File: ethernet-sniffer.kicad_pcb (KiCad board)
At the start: 4 copper layers, 120 x 117 mm, 320 parts, among them J1001 RJMG1BD3B8K1ANR, J101 Conn_01x06, J102 USB_B_Micro, J103 POWER 5V, J1101 RJMG1BD3B8K1ANR, J601 BOOT0, J602 BOOT1, J603 Debug Header, J606 Exension Port D, J701 JTAG, J801 RJMG1BD3B8K1ANR, J901 RJMG1BD3B8K1ANR, Q201 2N3904, Q202 2N3904, Q701 2N3904, SW601 SW_Push, SW701 RESET, U1001 AMS1117-3.3, U1002 DP83848C, U1101 AMS1117-3.3, U1102 DP83848C, U501 CH340G, U601 AMS1117-3.3, U602 STM32F107VCTx, U701 LM317_3PinPackage, U702 AMS1117-3.3, U707 XC6SLX9-TQG144, U708 W25Q128JVS, U801 AMS1117-3.3, U802 DP83848C, U901 AMS1117-3.3, U902 DP83848C, Y501 12MHz, Y601 25MHz

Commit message: Cleanup
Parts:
- added REF**: OSHW-Logo2_36.5x30mm_SilkScreen, Symbol:OSHW-Logo2_36.5x30mm_SilkScreen, B.Cu at (114.2, 125.2)
- J101: value Conn_01x06 -> Conn_01x08; footprint Connector_PinHeader_2.54mm:PinHeader_1x06_P2.54mm_Vertical -> Connector_PinHeader_2.54mm:PinHeader_1x08_P2.54mm_Vertical
- moved J101 17.8 mm to (210.0, 100.2), turned to 0 degrees
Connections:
- J101 pad 1: /STM32/UART_TX -> GNDD
- J101 pad 2: /STM32/UART_RX -> /STM32/STM_3V3
- J101 pad 3: /STM32/ADC1 -> /STM32/I2C_SCL
- J101 pad 4: /STM32/ADC2 -> /STM32/I2C_SDA
- J101 pad 5: /STM32/I2C_SDA -> /STM32/ADC2
- J101 pad 6: /STM32/I2C_SCL -> /STM32/ADC1
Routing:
- net /STM32/I2C_SDA: track 39.7 -> 34.6 mm
- net /STM32/STM_3V3: track 39.2 -> 44.0 mm
- net /STM32/I2C_SCL: track 37.3 -> 39.6 mm
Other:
- board text added: "3V3"
- board text added: "ADC1"
- board text added: "ADC2"
- board text added: "BOOT0"
- board text added: "BOOT1"
- board text added: "Christopher Simon"
- board text added: "Ethernet Sniffer v0.01"
- board text added: "FPGA 100BASE-TX 1"
- board text added: "FPGA 100BASE-TX 2"
- board text added: "FPGA 100BASE-TX 3"
- board text added: "GND"
- board text added: "JTAG"
- board text added: "PD0-7"
- board text added: "SDA"
- board text added: "SDL"
- board text added: "STM32 100BASE-TX"
- board text added: "SWD"
- board text added: "UART RX"
- board text added: "UART TX"

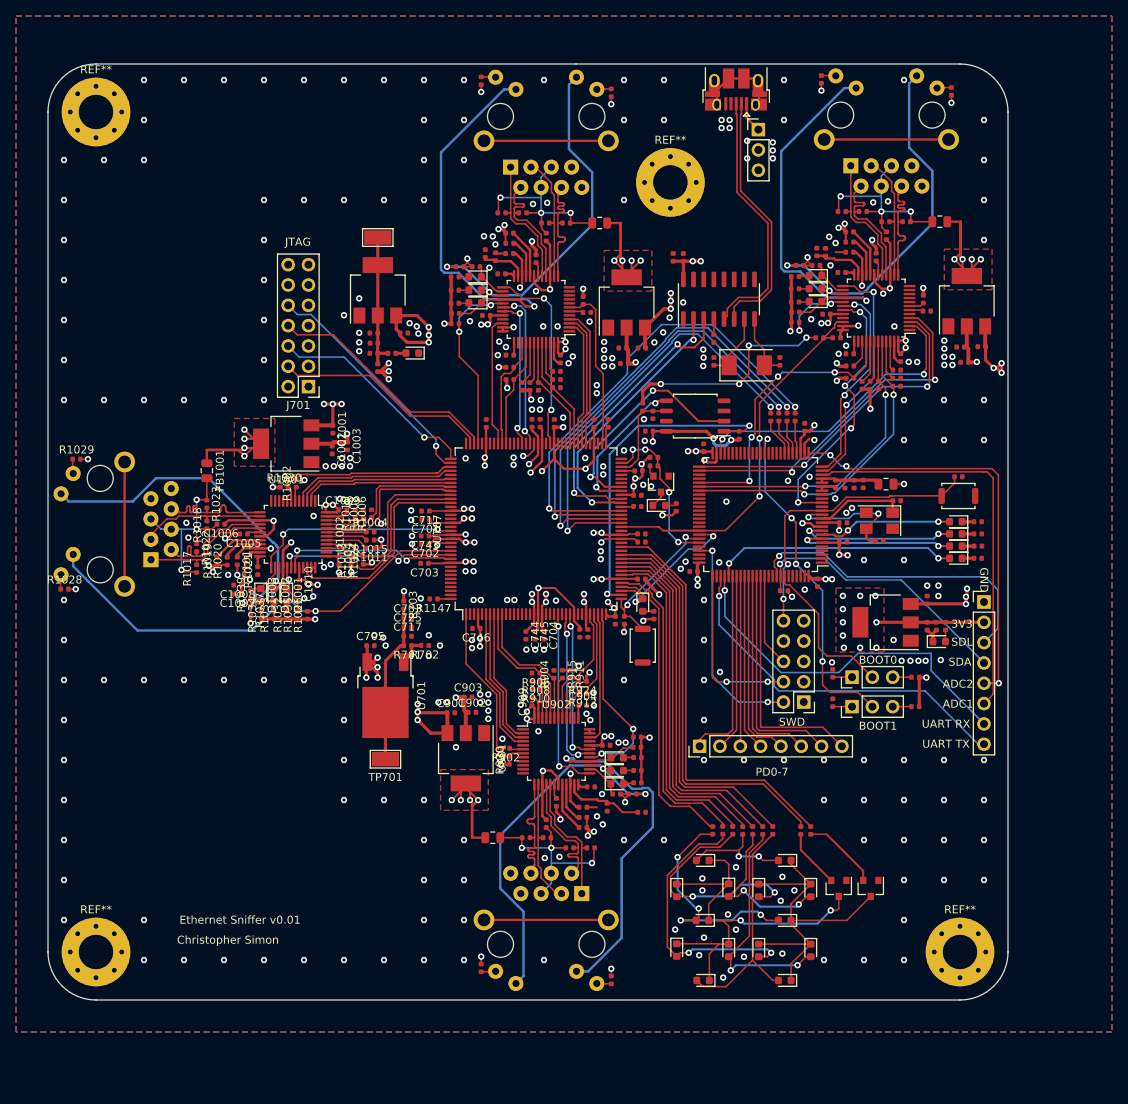
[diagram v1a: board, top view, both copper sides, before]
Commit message: PCB layout 90% finished
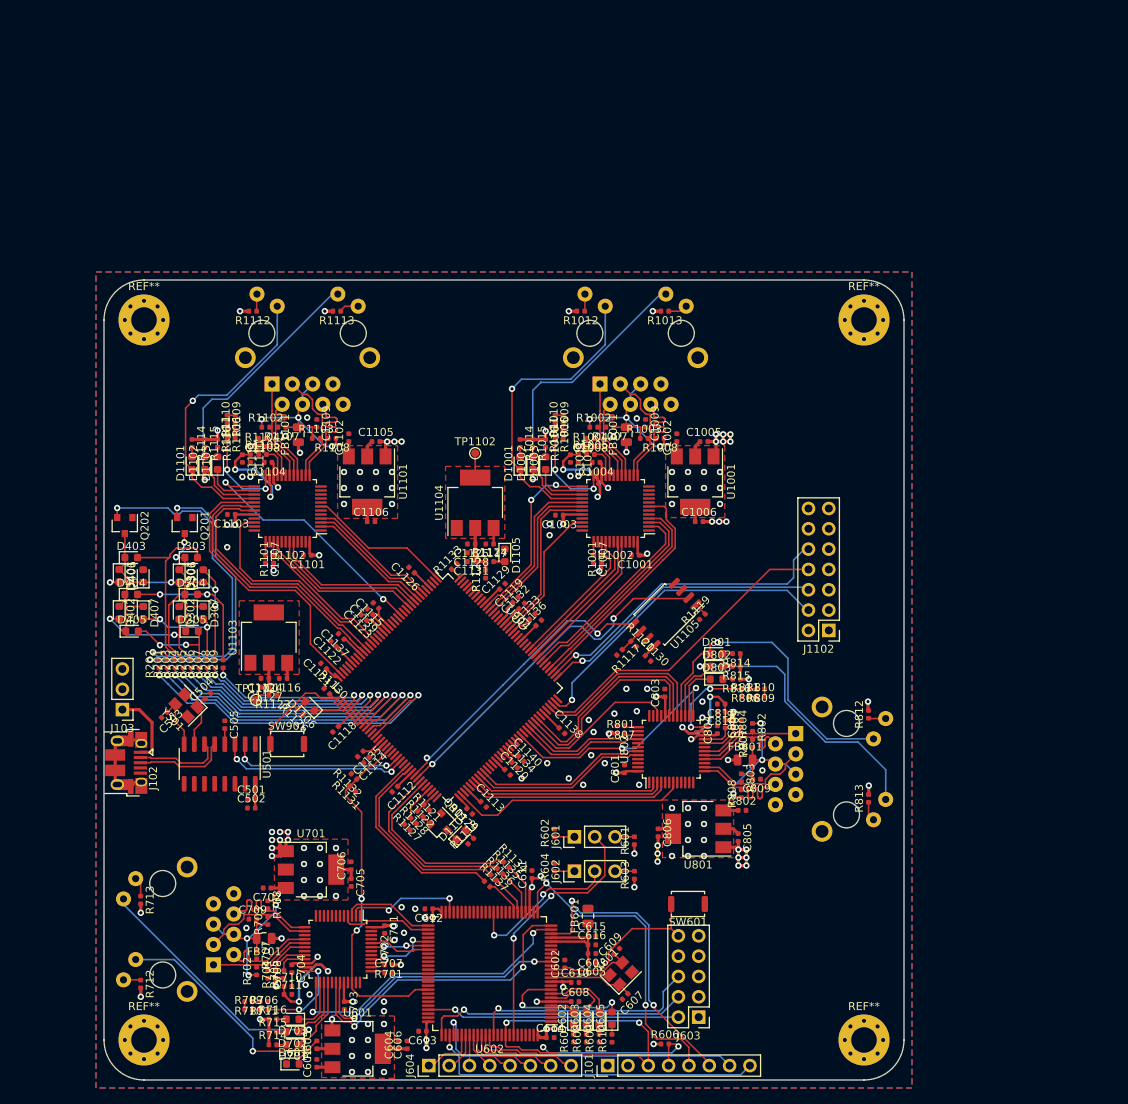
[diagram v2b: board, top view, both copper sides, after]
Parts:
- removed C1012, C712, C713, C714, C715, C716, C723, C724, C732, C740, C741, C743, C744, C745, C746, C747, C748, C903, C904, C905, C906, C907, C909, C910, C911: 100n, Capacitor_SMD:C_0402_1005Metric
- removed C717, C718, C901, C908: 10u, Capacitor_SMD:C_0402_1005Metric
- removed C725, C726: 4u7, Capacitor_SMD:C_0402_1005Metric
- removed C733, C734: 470n, Capacitor_SMD:C_0402_1005Metric
- removed C902: 1u, Capacitor_SMD:C_0402_1005Metric
- removed D706, D707: INIT, LED_SMD:LED_0603_1608Metric
- removed D901: LINK, LED_SMD:LED_0603_1608Metric
- removed D902: SPEED, LED_SMD:LED_0603_1608Metric
- removed D903: ACT, LED_SMD:LED_0603_1608Metric
- removed FB901: Bead, Inductor_SMD:L_0805_2012Metric
- removed J606: Exension Port D, Connector_PinHeader_2.54mm:PinHeader_1x08_P2.54mm_Vertical
- removed J901: RJMG1BD3B8K1ANR, Connector_RJ:RJ45_Amphenol_RJMG1BD3B8K1ANR
- removed Q701: 2N3904, Package_TO_SOT_SMD:SOT-23
- removed R1017, R1018, R1022, R1023, R817, R818, R822, R823, R917, R918, R922, R923: 50, Resistor_SMD:R_0402_1005Metric
- removed R1019, R1020, R1024, R1026, R1030, R1035, R1037, R1039, R1139, R1147, R1148, R719, R721, R722, R723, R819, R820, R824, R826, R830, R835, R837, R839, R902, R904, R906, R908, R910, R911, R913, R915, R919, R920, R924, R926, R930, R935, R937, R939: 2k2, Resistor_SMD:R_0402_1005Metric
- removed R1021, R821, R921: 4k87, Resistor_SMD:R_0402_1005Metric
- removed R1028, R1029, R1032, R1033, R1034, R720, R828, R829, R832, R833, R834, R928, R929, R932, R933, R934: 200, Resistor_SMD:R_0402_1005Metric
- removed R1141, R1142, R717: 100, Resistor_SMD:R_0402_1005Metric
- removed R1143, R1144, R1145, R1146: 1k, Resistor_SMD:R_0402_1005Metric
- removed R718: 10k, Resistor_SMD:R_0402_1005Metric
- removed the REF** at (114.2, 125.2)
- removed the REF** at (170.8, 47.8)
- removed the REF** at (207.0, 144.0)
- removed the REF** at (99.0, 144.0)
- removed the REF** at (99.0, 39.0)
- removed SW701: RESET, Button_Switch_SMD:SW_Push_SPST_NO_Alps_SKRK
- removed TP701: TP 1.2V VCCINT, TestPoint:TestPoint_Keystone_5015_Micro-Minature
- removed TP702: TP 3.3V VCCAUX, TestPoint:TestPoint_Keystone_5015_Micro-Minature
- removed U707: XC6SLX9-TQG144, Package_QFP:LQFP-144_20x20mm_P0.5mm
- removed U708: W25Q128JVS, Package_SO:SOIC-8_5.23x5.23mm_P1.27mm
- removed U901: AMS1117-3.3, Package_TO_SOT_SMD:SOT-223-3_TabPin2
- removed U902: DP83848C, Package_QFP:LQFP-48_7x7mm_P0.5mm
- added C1112: 100n, Capacitor_SMD:C_0402_1005Metric, F.Cu at (136.4, 123.6)
- added C1113: 100n, Capacitor_SMD:C_0402_1005Metric, F.Cu at (147.4, 125.5)
- added C1114: 100n, Capacitor_SMD:C_0402_1005Metric, F.Cu at (132.8, 120.0)
- added C1115: 100n, Capacitor_SMD:C_0402_1005Metric, F.Cu at (134.0, 100.7)
- added C1116: 4u7, Capacitor_SMD:C_0402_1005Metric, F.Cu at (122.4, 109.8)
- added C1117: 4u7, Capacitor_SMD:C_0402_1005Metric, F.Cu at (148.2, 93.0)
- added C1118: 100n, Capacitor_SMD:C_0402_1005Metric, F.Cu at (128.9, 116.2)
- added C1119: 100n, Capacitor_SMD:C_0402_1005Metric, F.Cu at (151.4, 100.0)
- added C1120: 100n, Capacitor_SMD:C_0402_1005Metric, F.Cu at (150.4, 121.5)
- added C1121: 100n, Capacitor_SMD:C_0402_1005Metric, F.Cu at (127.5, 108.3)
- added C1122: 100n, Capacitor_SMD:C_0402_1005Metric, F.Cu at (128.7, 105.5)
- added C1123: 100n, Capacitor_SMD:C_0402_1005Metric, F.Cu at (132.5, 102.2)
- added C1124: 10u, Capacitor_SMD:C_0402_1005Metric, F.Cu at (120.1, 109.8)
- added C1125: 10u, Capacitor_SMD:C_0402_1005Metric, F.Cu at (145.9, 93.0)
- added C1126: 100n, Capacitor_SMD:C_0402_1005Metric, F.Cu at (138.5, 96.3)
- added C1127: 4u7, Capacitor_SMD:C_0402_1005Metric, F.Cu at (120.1, 110.9)
- added C1128: 4u7, Capacitor_SMD:C_0402_1005Metric, F.Cu at (145.9, 94.1)
- added C1129: 100n, Capacitor_SMD:C_0402_1005Metric, F.Cu at (149.8, 98.3)
- added C1130: 100n, Capacitor_SMD:C_0402_1005Metric, F.Cu at (168.0, 107.3)
- added C1131: 470n, Capacitor_SMD:C_0402_1005Metric, F.Cu at (145.9, 95.2)
- added C1132: 100n, Capacitor_SMD:C_0402_1005Metric, F.Cu at (152.2, 100.8)
- added C1133: 100n, Capacitor_SMD:C_0402_1005Metric, F.Cu at (153.5, 102.1)
- added C1134: 100n, Capacitor_SMD:C_0402_1005Metric, F.Cu at (151.3, 120.6)
- added C1135: 100n, Capacitor_SMD:C_0402_1005Metric, F.Cu at (132.1, 119.2)
- added C1136: 100n, Capacitor_SMD:C_0402_1005Metric, F.Cu at (154.3, 102.9)
- added C1137: 100n, Capacitor_SMD:C_0402_1005Metric, F.Cu at (129.7, 104.6)
- added C1138: 100n, Capacitor_SMD:C_0402_1005Metric, F.Cu at (157.2, 116.3)
- added C1139: 100n, Capacitor_SMD:C_0402_1005Metric, F.Cu at (133.3, 101.5)
- added C1140: 100n, Capacitor_SMD:C_0402_1005Metric, F.Cu at (152.1, 119.8)
- added C707: 100n, Capacitor_SMD:C_0402_1005Metric, F.Cu at (135.6, 146.6)
- added C708: 100n, Capacitor_SMD:C_0402_1005Metric, F.Cu at (120.5, 146.8)
- added C709: 100n, Capacitor_SMD:C_0402_1005Metric, F.Cu at (118.6, 139.9)
- added C710: 100n, Capacitor_SMD:C_0402_1005Metric, F.Cu at (123.0, 148.3)
- added D1104: INIT, LED_SMD:LED_0603_1608Metric, F.Cu at (144.7, 129.3)
- added D1105: LED_Small, LED_SMD:LED_0603_1608Metric, F.Cu at (150.1, 94.4)
- added D1106: INIT, LED_SMD:LED_0603_1608Metric, F.Cu at (125.7, 113.2)
- added D702: SPEED, LED_SMD:LED_0603_1608Metric, F.Cu at (123.6, 154.0)
- added D703: ACT, LED_SMD:LED_0603_1608Metric, F.Cu at (123.6, 152.4)
- added FB701: Bead, Inductor_SMD:L_0805_2012Metric, F.Cu at (120.0, 142.3)
- added J1102: JTAG, Connector_PinHeader_2.54mm:PinHeader_2x07_P2.54mm_Vertical, F.Cu at (190.6, 103.8)
- added J604: Exension Port D, Connector_PinHeader_2.54mm:PinHeader_1x08_P2.54mm_Vertical, F.Cu at (140.6, 158.2)
- added Q901: 2N3904, Package_TO_SOT_SMD:SOT-23, F.Cu at (142.2, 128.0)
- added R1001: 2k2, Resistor_SMD:R_0402_1005Metric, F.Cu at (162.2, 94.9)
- added R1003: 49.9, Resistor_SMD:R_0402_1005Metric, F.Cu at (167.5, 79.8)
- added R1005: 2k2, Resistor_SMD:R_0402_1005Metric, F.Cu at (160.8, 81.8)
- added R1007: 49.9, Resistor_SMD:R_0402_1005Metric, F.Cu at (163.2, 78.4)
- added R1009: 150, Resistor_SMD:R_0402_1005Metric, F.Cu at (156.4, 77.4)
- added R1012: 200, Resistor_SMD:R_0402_1005Metric, F.Cu at (159.6, 63.9)
- added R1014: 200, Resistor_SMD:R_0402_1005Metric, F.Cu at (152.0, 80.4)
- added R1016: 200, Resistor_SMD:R_0402_1005Metric, F.Cu at (155.2, 80.4)
- added R1101: 2k2, Resistor_SMD:R_0402_1005Metric, F.Cu at (121.2, 94.9)
- added R1103: 49.9, Resistor_SMD:R_0402_1005Metric, F.Cu at (126.5, 79.8)
- added R1105: 2k2, Resistor_SMD:R_0402_1005Metric, F.Cu at (119.8, 81.8)
- added R1107: 49.9, Resistor_SMD:R_0402_1005Metric, F.Cu at (122.2, 78.4)
- added R1109: 150, Resistor_SMD:R_0402_1005Metric, F.Cu at (115.4, 77.4)
- added R1112: 200, Resistor_SMD:R_0402_1005Metric, F.Cu at (118.6, 63.9)
- added R1114: 200, Resistor_SMD:R_0402_1005Metric, F.Cu at (111.0, 80.4)
- added R1116: 200, Resistor_SMD:R_0402_1005Metric, F.Cu at (114.2, 80.4)
- added R1125: 0, Resistor_SMD:R_0402_1005Metric, F.Cu at (147.7, 96.8)
- added R1127: 2k2, Resistor_SMD:R_0402_1005Metric, F.Cu at (138.7, 127.6)
- added R1131: 100, Resistor_SMD:R_0402_1005Metric, F.Cu at (131.1, 123.6)
- added R1136: 1k, Resistor_SMD:R_0402_1005Metric, F.Cu at (148.7, 134.7)
- added R705: 2k2, Resistor_SMD:R_0402_1005Metric, F.Cu at (122.5, 146.8)
- added R706: 4k7, Resistor_SMD:R_0402_1005Metric, F.Cu at (120.0, 151.2)
- added R707: 49.9, Resistor_SMD:R_0402_1005Metric, F.Cu at (119.1, 144.4)
- added R708: 49.9, Resistor_SMD:R_0402_1005Metric, F.Cu at (120.5, 138.1)
- added R709: 150, Resistor_SMD:R_0402_1005Metric, F.Cu at (118.1, 151.2)
- added R710: 10, Resistor_SMD:R_0402_1005Metric, F.Cu at (118.1, 150.2)
- added R711: 10, Resistor_SMD:R_0402_1005Metric, F.Cu at (120.0, 150.2)
- added R712: 200, Resistor_SMD:R_0402_1005Metric, F.Cu at (104.6, 148.0)
- added R801: 2k2, Resistor_SMD:R_0402_1005Metric, F.Cu at (164.6, 116.7)
- added R803: 49.9, Resistor_SMD:R_0402_1005Metric, F.Cu at (179.7, 122.2)
- added R805: 2k2, Resistor_SMD:R_0402_1005Metric, F.Cu at (177.7, 115.5)
- added R807: 49.9, Resistor_SMD:R_0402_1005Metric, F.Cu at (181.1, 117.9)
- added R809: 150, Resistor_SMD:R_0402_1005Metric, F.Cu at (182.1, 111.1)
- added R812: 200, Resistor_SMD:R_0402_1005Metric, F.Cu at (195.6, 114.3)
- added R814: 200, Resistor_SMD:R_0402_1005Metric, F.Cu at (179.1, 106.7)
- added R816: 200, Resistor_SMD:R_0402_1005Metric, F.Cu at (179.1, 109.9)
- added REF**: MountingHole_3.2mm_M3_Pad_Via, MountingHole:MountingHole_3.2mm_M3_Pad_Via, F.Cu at (195.0, 155.0)
- added REF**: MountingHole_3.2mm_M3_Pad_Via, MountingHole:MountingHole_3.2mm_M3_Pad_Via, F.Cu at (105.0, 155.0)
- added REF**: MountingHole_3.2mm_M3_Pad_Via, MountingHole:MountingHole_3.2mm_M3_Pad_Via, F.Cu at (105.0, 65.0)
- added REF**: MountingHole_3.2mm_M3_Pad_Via, MountingHole:MountingHole_3.2mm_M3_Pad_Via, F.Cu at (195.0, 65.0)
- added SW901: RESET, Button_Switch_SMD:SW_Push_SPST_NO_Alps_SKRK, F.Cu at (122.9, 118.0)
- added TP1101: TP 1.2V VCCINT, TestPoint:TestPoint_Pad_D1.0mm, F.Cu at (119.0, 112.5)
- added TP1102: TP 3.3V VCCAUX, TestPoint:TestPoint_Pad_D1.0mm, F.Cu at (146.4, 81.7)
- added U1103: SE1122-LF-1.2V, Package_TO_SOT_SMD:SOT-223-3_TabPin2, F.Cu at (120.6, 104.7)
- added U1104: AMS1117-3.3, Package_TO_SOT_SMD:SOT-223-3_TabPin2, F.Cu at (146.4, 87.8)
- added U1105: W25Q128JVS, Package_SO:SOIC-8_5.23x5.23mm_P1.27mm, F.Cu at (170.1, 101.8)
- added U904: XC6SLX9-TQG144, Package_QFP:LQFP-144_20x20mm_P0.5mm, F.Cu at (143.0, 111.0)
- C1001, C1008, C1101, C1108, C801, C808: value 10u -> 100n
- C1005, C1105, C702, C805: value 100n -> 1u
- C1011, C1111, C711, C811: value 100n -> 10u
- C601, C604: value 10u -> 1u
- C606: value 1u -> 10n
- C705: value 4u7 -> 1u
- C706: value 4u7 -> 100n
- D701: value LED_Small -> LINK
- J701: value JTAG -> RJMG1BD3B8K1ANR; footprint Connector_PinHeader_2.54mm:PinHeader_2x07_P2.54mm_Vertical -> Connector_RJ:RJ45_Amphenol_RJMG1BD3B8K1ANR; moved to B.Cu
- R1002, R1008, R1102, R1108, R802, R808: value 2k2 -> 49.9
- R1006, R1106, R806: value 2k2 -> 4k7
- R1010, R1011, R1110, R1111, R810, R811: value 2k2 -> 10
- R1013, R1015, R1113, R1115, R1119, R1124, R1126, R813, R815: value 2k2 -> 200
- R1117: value 50 -> 100
- R1118: value 50 -> 200
- R1120: value 2k2 -> 100
- R1121: value 4k87 -> 10k
- R1122: value 50 -> 2k2
- R1123: value 50 -> 0
- R1128, R1129, R1133, R704: value 200 -> 2k2
- R1132: value 200 -> 100
- R1134: value 200 -> 1k
- R1135, R1137: value 2k2 -> 1k
- R701: value 0 -> 2k2
- R702: value 1M -> 49.9
- R703: value 0 -> 49.9
- R713: value 0 -> 200
- R714: value 100 -> 200
- U701: value LM317_3PinPackage -> AMS1117-3.3; footprint Package_TO_SOT_SMD:TO-252-2 -> Package_TO_SOT_SMD:SOT-223-3_TabPin2
- U702: value AMS1117-3.3 -> DP83848C; footprint Package_TO_SOT_SMD:SOT-223-3_TabPin2 -> Package_QFP:LQFP-48_7x7mm_P0.5mm
- Y501: value 12MHz -> X322512MSB4SI 12MHZ; footprint Crystal:Crystal_SMD_0603-2Pin_6.0x3.5mm -> Crystal:Crystal_SMD_3225-4Pin_3.2x2.5mm
- Y601: value 25MHz -> X322525MOB4SI 25MHZ; footprint Crystal:Crystal_SMD_5032-4Pin_5.0x3.2mm -> Crystal:Crystal_SMD_3225-4Pin_3.2x2.5mm
- moved J102 113.5 mm to (102.8, 120.4), turned to 270 degrees
- moved J103 107.6 mm to (102.3, 113.7), turned to 180 degrees
- moved Q202 100.1 mm to (102.6, 90.7)
- moved Q201 97.0 mm to (110.1, 90.7)
- moved D601 96.5 mm to (123.6, 158.0)
- moved C601 95.8 mm to (126.6, 157.9)
- moved R605 94.4 mm to (126.6, 155.6), turned to 90 degrees
- moved R1128 93.8 mm to (137.9, 128.4), turned to 315 degrees
- moved R716 93.4 mm to (121.1, 152.4), turned to 0 degrees
- moved R714 92.2 mm to (121.1, 155.6), turned to 0 degrees
- moved D301 91.8 mm to (109.4, 97.0)
- moved R1129 91.5 mm to (145.7, 126.4), turned to 135 degrees
- moved D303 91.1 mm to (110.9, 94.7), turned to 0 degrees
- moved D401 89.4 mm to (101.9, 97.0)
- moved D403 88.9 mm to (103.4, 94.7), turned to 0 degrees
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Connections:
- C1001 pad 1: +5V -> /PHY2/PHY_3V3
- C1002 pad 1: /PHY2/PHY_3V3 -> +5V
- C1004 pad 1: Net-(C1004-Pad1) -> /PHY2/PHY_3V3
- C1005 pad 1: Net-(C1005-Pad1) -> /PHY2/PHY_3V3
- C1006 pad 1: GNDD -> /PHY2/PHY_3V3
- C1006 pad 2: Net-(C1006-Pad2) -> GNDD
- C1008 pad 1: Net-(C1007-Pad1) -> Net-(C1008-Pad1)
- C1009 pad 1: /PHY2/PHY_3V3 -> GNDD
- C1009 pad 2: GNDD -> Net-(C1009-Pad2)
- C1010 pad 1: /PHY2/PHY_3V3 -> Net-(C1010-Pad1)
- C1011 pad 1: /PHY2/PHY_3V3 -> Net-(C1010-Pad1)
- C1101 pad 1: +5V -> /PHY1/PHY_3V3
- C1102 pad 1: /PHY3/PHY_3V3 -> +5V
- C1103 pad 1: /PHY3/PHY_3V3 -> /PHY1/PHY_3V3
- C1104 pad 1: Net-(C1104-Pad1) -> /PHY1/PHY_3V3
- C1105 pad 1: Net-(C1105-Pad1) -> /PHY1/PHY_3V3
- C1106 pad 1: GNDD -> /PHY1/PHY_3V3
- C1106 pad 2: Net-(C1106-Pad2) -> GNDD
- C1108 pad 1: Net-(C1107-Pad1) -> Net-(C1108-Pad1)
- C1109 pad 1: /PHY3/PHY_3V3 -> GNDD
- C1109 pad 2: GNDD -> Net-(C1109-Pad2)
- C1110 pad 1: /PHY3/PHY_3V3 -> Net-(C1110-Pad1)
- C1111 pad 1: /PHY3/PHY_3V3 -> Net-(C1110-Pad1)
- C701 pad 1: /FPGA/VCCO_3V3 -> /100BASETX-PHY 1/PHY_3V3
- C702 pad 1: /FPGA/VCCO_3V3 -> +5V
- C703 pad 1: /FPGA/VCCO_3V3 -> /100BASETX-PHY 1/PHY_3V3
- C704 pad 1: /FPGA/VCCO_3V3 -> /100BASETX-PHY 1/PHY_3V3
- C705 pad 1: +5V -> /100BASETX-PHY 1/PHY_3V3
- C706 pad 1: +5V -> /100BASETX-PHY 1/PHY_3V3
- C711 pad 1: /FPGA/VCCO_3V3 -> Net-(C710-Pad1)
- C801 pad 1: +5V -> /PHY3/PHY_3V3
- C802 pad 1: /100BASETX-PHY 1/PHY_3V3 -> +5V
- C803 pad 1: /100BASETX-PHY 1/PHY_3V3 -> /PHY3/PHY_3V3
- C804 pad 1: Net-(C804-Pad1) -> /PHY3/PHY_3V3
- C805 pad 1: Net-(C805-Pad1) -> /PHY3/PHY_3V3
- C806 pad 1: GNDD -> /PHY3/PHY_3V3
- C806 pad 2: Net-(C806-Pad2) -> GNDD
- C808 pad 1: Net-(C807-Pad1) -> Net-(C808-Pad1)
- C809 pad 1: /100BASETX-PHY 1/PHY_3V3 -> GNDD
- C809 pad 2: GNDD -> Net-(C809-Pad2)
- C810 pad 1: /100BASETX-PHY 1/PHY_3V3 -> Net-(C810-Pad1)
- C811 pad 1: /100BASETX-PHY 1/PHY_3V3 -> Net-(C810-Pad1)
- D1101 pad 1: /PHY3/AN0 -> /PHY1/AN0
- D1102 pad 1: /PHY3/AN1 -> /PHY1/AN1
- D1103 pad 1: /PHY3/AN_EN -> /PHY1/AN_EN
- D701 pad 1: GNDD -> /100BASETX-PHY 1/AN0
- D801 pad 1: /100BASETX-PHY 1/AN0 -> /PHY3/AN0
- D802 pad 1: /100BASETX-PHY 1/AN1 -> /PHY3/AN1
- D803 pad 1: /100BASETX-PHY 1/AN_EN -> /PHY3/AN_EN
- FB1001 pad 2: Net-(C1006-Pad2) -> Net-(C1009-Pad2)
- FB1101 pad 1: /PHY3/PHY_3V3 -> /PHY1/PHY_3V3
- FB1101 pad 2: Net-(C1106-Pad2) -> Net-(C1109-Pad2)
- FB801 pad 1: /100BASETX-PHY 1/PHY_3V3 -> /PHY3/PHY_3V3
- FB801 pad 2: Net-(C806-Pad2) -> Net-(C809-Pad2)
- J1001 pad R4: Net-(C1006-Pad2) -> Net-(C1009-Pad2)
- J1001 pad R5: Net-(C1006-Pad2) -> Net-(C1009-Pad2)
- J1101 pad L2: /PHY3/AN1 -> /PHY1/AN1
- J1101 pad L3: /PHY3/AN0 -> /PHY1/AN0
- J1101 pad R1: /PHY3/TD+ -> /PHY1/TD+
- J1101 pad R2: /PHY3/TD- -> /PHY1/TD-
- J1101 pad R3: /PHY3/RX+ -> /PHY1/RX+
- J1101 pad R4: Net-(C1106-Pad2) -> Net-(C1109-Pad2)
- J1101 pad R5: Net-(C1106-Pad2) -> Net-(C1109-Pad2)
- J1101 pad R6: /PHY3/RX- -> /PHY1/RX-
- J701 pad 13: GNDD -> Net-(J701-Pad13)
- J801 pad L2: /100BASETX-PHY 1/AN1 -> /PHY3/AN1
- J801 pad L3: /100BASETX-PHY 1/AN0 -> /PHY3/AN0
- J801 pad R1: /100BASETX-PHY 1/TD+ -> /PHY3/TD+
- J801 pad R2: /100BASETX-PHY 1/TD- -> /PHY3/TD-
- J801 pad R3: /100BASETX-PHY 1/RX+ -> /PHY3/RX+
- J801 pad R4: Net-(C806-Pad2) -> Net-(C809-Pad2)
- J801 pad R5: Net-(C806-Pad2) -> Net-(C809-Pad2)
- J801 pad R6: /100BASETX-PHY 1/RX- -> /PHY3/RX-
- R1002 pad 1: /PHY2/SNI_MODE -> Net-(C1009-Pad2)
- R1002 pad 2: GNDD -> /PHY2/TD+
- R1004 pad 1: /FPGA/PHY2_RXD_0 -> /PHY2/PHY_3V3
- R1004 pad 2: GNDD -> Net-(R1004-Pad2)
- R1006 pad 1: /FPGA/PHY2_RXD_1 -> Net-(R1006-Pad1)
- R1006 pad 2: GNDD -> Net-(R1006-Pad2)
- R1008 pad 1: /PHY2/PHY_AD3 -> Net-(C1009-Pad2)
- R1008 pad 2: GNDD -> /PHY2/RX-
- R1010 pad 1: /PHY2/PHY_AD4 -> Net-(R1010-Pad1)
- R1010 pad 2: GNDD -> Net-(R1009-Pad1)
- R1011 pad 1: /PHY2/PHY_3V3 -> GNDD
- R1011 pad 2: /PHY2/MDIX_EN -> Net-(R1010-Pad1)
- R1013 pad 1: /PHY2/PHY_3V3 -> Net-(J1001-PadL1)
- R1013 pad 2: /FPGA/PHY2_RX_DV -> /PHY2/PHY_3V3
- R1015 pad 2: /PHY2/PHY_AD0 -> Net-(D1002-Pad2)
- R1102 pad 1: /PHY3/SNI_MODE -> Net-(C1109-Pad2)
- R1102 pad 2: GNDD -> /PHY1/TD+
- R1104 pad 1: /FPGA/PHY3_RXD_0 -> /PHY1/PHY_3V3
- R1104 pad 2: GNDD -> Net-(R1104-Pad2)
- R1106 pad 1: /FPGA/PHY3_RXD_1 -> Net-(R1106-Pad1)
- R1106 pad 2: GNDD -> Net-(R1106-Pad2)
- R1108 pad 1: /PHY3/PHY_AD3 -> Net-(C1109-Pad2)
- R1108 pad 2: GNDD -> /PHY1/RX-
- R1110 pad 1: /PHY3/PHY_AD4 -> Net-(R1110-Pad1)
- R1110 pad 2: GNDD -> Net-(R1109-Pad1)
- R1111 pad 1: /PHY3/PHY_3V3 -> GNDD
- R1111 pad 2: /PHY3/MDIX_EN -> Net-(R1110-Pad1)
- R1113 pad 1: /PHY3/PHY_3V3 -> Net-(J1101-PadL1)
- R1113 pad 2: /FPGA/PHY3_RX_DV -> /PHY1/PHY_3V3
- R1115 pad 1: /PHY3/PHY_3V3 -> /PHY1/PHY_3V3
- R1115 pad 2: /PHY3/PHY_AD0 -> Net-(D1102-Pad2)
- R1117 pad 1: Net-(C1106-Pad2) -> /FPGA/CCLK
- R1117 pad 2: /PHY3/TD+ -> /FPGA/VCCO_3V3
- R1118 pad 1: Net-(C1106-Pad2) -> /FPGA/VCCO_3V3
- R1118 pad 2: /PHY3/RX+ -> Net-(D1104-Pad2)
- R1119 pad 1: /PHY3/PHY_3V3 -> /FPGA/VCCO_3V3
- R1119 pad 2: Net-(R1119-Pad2) -> /FPGA/CSO_B
- R1120 pad 1: /PHY3/PHY_3V3 -> /FPGA/CCLK
- R1120 pad 2: Net-(R1120-Pad2) -> GNDD
- R1121 pad 1: GNDD -> /FPGA/DONE
- R1121 pad 2: Net-(R1121-Pad2) -> Net-(Q901-Pad2)
- R1122 pad 1: Net-(C1106-Pad2) -> /FPGA/VCCO_3V3
- R1122 pad 2: /PHY3/TD- -> /FPGA/DONE
- R1123 pad 1: Net-(C1106-Pad2) -> /FPGA/VCCINT_1V2
- R1123 pad 2: /PHY3/RX- -> Net-(C1124-Pad1)
- R1124 pad 1: /PHY3/PHY_3V3 -> Net-(C1125-Pad1)
- R1124 pad 2: /PHY3/CRS_DV -> Net-(D1105-Pad2)
- R1126 pad 1: /PHY3/PHY_3V3 -> /FPGA/VCCO_3V3
- R1126 pad 2: /FPGA/~PHY3_RESET -> Net-(D1106-Pad2)
- R1128 pad 1: Net-(J1101-PadL4) -> /FPGA/M1
- R1128 pad 2: /PHY3/PHY_3V3 -> GNDD
- R1129 pad 1: Net-(J1101-PadL1) -> GNDD
- R1129 pad 2: /PHY3/PHY_3V3 -> Net-(R1129-Pad2)
- R1130 pad 1: /PHY3/PHY_3V3 -> /FPGA/VCCO_3V3
- R1130 pad 2: /FPGA/PHY3_POWER_DOWN -> /STM32/FPGA_PROGRAM
- R1132 pad 1: /PHY3/PHY_3V3 -> /FPGA/CLK_IN
- R1132 pad 2: Net-(D1101-Pad2) -> GNDD
- R1133 pad 1: /PHY3/PHY_3V3 -> Net-(R1133-Pad1)
- R1133 pad 2: Net-(D1102-Pad2) -> GNDD
- R1134 pad 1: /PHY3/PHY_3V3 -> Net-(R1134-Pad1)
- R1134 pad 2: Net-(D1103-Pad2) -> /STM32/SPI1_CS
- R1135 pad 1: /PHY3/PHY_3V3 -> Net-(R1135-Pad1)
- R1135 pad 2: /PHY3/AN0 -> /STM32/SPI1_SCK
- R1137 pad 1: /PHY3/PHY_3V3 -> Net-(R1137-Pad1)
- R1137 pad 2: /PHY3/AN1 -> /STM32/SPI1_MOSI
- R701 pad 1: Net-(R701-Pad1) -> /100BASETX-PHY 1/PHY_3V3
- R701 pad 2: Net-(C717-Pad1) -> /100BASETX-PHY 1/RX_DV
- R702 pad 1: GNDD -> Net-(C709-Pad2)
- R702 pad 2: Net-(R701-Pad1) -> /100BASETX-PHY 1/TD+
- R703 pad 1: /FPGA/VCCINT_1V2 -> Net-(C709-Pad2)
- R703 pad 2: Net-(C717-Pad1) -> /100BASETX-PHY 1/RX+
- R704 pad 1: Net-(C718-Pad1) -> /100BASETX-PHY 1/PHY_3V3
- R704 pad 2: Net-(D701-Pad2) -> Net-(R704-Pad2)
- R713 pad 1: /FPGA/VCCO_3V3 -> Net-(J701-PadL1)
- R713 pad 2: Net-(C718-Pad1) -> /100BASETX-PHY 1/PHY_3V3
- R714 pad 1: /FPGA/CCLK -> /100BASETX-PHY 1/PHY_3V3
- R714 pad 2: /FPGA/VCCO_3V3 -> Net-(D701-Pad2)
- R715 pad 1: /FPGA/VCCO_3V3 -> /100BASETX-PHY 1/PHY_3V3
- R716 pad 1: /FPGA/VCCO_3V3 -> /100BASETX-PHY 1/PHY_3V3
- R716 pad 2: /FPGA/CSO_B -> Net-(D703-Pad2)
- R802 pad 1: /100BASETX-PHY 1/SNI_MODE -> Net-(C809-Pad2)
- R802 pad 2: GNDD -> /PHY3/TD+
- R804 pad 1: /STM32/PHY_RXD_0 -> /PHY3/PHY_3V3
- R804 pad 2: GNDD -> Net-(R804-Pad2)
- R806 pad 1: /STM32/PHY_RXD_1 -> Net-(R806-Pad1)
- R806 pad 2: GNDD -> Net-(R806-Pad2)
- R808 pad 1: /100BASETX-PHY 1/PHY_AD3 -> Net-(C809-Pad2)
- R808 pad 2: GNDD -> /PHY3/RX-
- R810 pad 1: /100BASETX-PHY 1/PHY_AD4 -> Net-(R810-Pad1)
- R810 pad 2: GNDD -> Net-(R809-Pad1)
- R811 pad 1: /100BASETX-PHY 1/PHY_3V3 -> GNDD
- R811 pad 2: /100BASETX-PHY 1/MDIX_EN -> Net-(R810-Pad1)
- R813 pad 1: /100BASETX-PHY 1/PHY_3V3 -> Net-(J801-PadL1)
- R813 pad 2: /100BASETX-PHY 1/RX_DV -> /PHY3/PHY_3V3
- R815 pad 1: /100BASETX-PHY 1/PHY_3V3 -> /PHY3/PHY_3V3
- R815 pad 2: /100BASETX-PHY 1/PHY_AD0 -> Net-(D802-Pad2)
- U1002 pad 18: Net-(C1005-Pad1) -> Net-(C1008-Pad1)
- U1002 pad 20: Net-(R1019-Pad2) -> Net-(R1004-Pad2)
- U1002 pad 23: Net-(C1007-Pad1) -> Net-(C1010-Pad1)
- U1002 pad 24: Net-(R1021-Pad2) -> Net-(R1006-Pad2)
- U1002 pad 37: Net-(C1004-Pad1) -> Net-(C1007-Pad1)
- U1101 pad 2: /PHY3/PHY_3V3 -> /PHY1/PHY_3V3
- U1102 pad 13: /PHY3/RX- -> /PHY1/RX-
- U1102 pad 14: /PHY3/RX+ -> /PHY1/RX+
- U1102 pad 16: /PHY3/TD- -> /PHY1/TD-
- U1102 pad 17: /PHY3/TD+ -> /PHY1/TD+
- U1102 pad 18: Net-(C1105-Pad1) -> Net-(C1108-Pad1)
- U1102 pad 2: /FPGA/PHY3_TX_EN -> /FPGA/PHY1_TX_EN
- U1102 pad 20: Net-(R1119-Pad2) -> Net-(R1104-Pad2)
- U1102 pad 21: Net-(R1120-Pad2) -> Net-(R1105-Pad2)
- U1102 pad 22: /PHY3/PHY_3V3 -> /PHY1/PHY_3V3
- U1102 pad 23: Net-(C1107-Pad1) -> Net-(C1110-Pad1)
- U1102 pad 24: Net-(R1121-Pad2) -> Net-(R1106-Pad2)
- U1102 pad 25: /PHY3/CLK_OUT -> /PHY1/CLK_OUT
- U1102 pad 26: /PHY3/AN_EN -> /PHY1/AN_EN
- U1102 pad 27: /PHY3/AN1 -> /PHY1/AN1
- U1102 pad 28: /PHY3/AN0 -> /PHY1/AN0
- U1102 pad 29: /FPGA/~PHY3_RESET -> /FPGA/~PHY1_RESET
- U1102 pad 3: /FPGA/PHY3_TXD_0 -> /FPGA/PHY1_TXD_0
- U1102 pad 30: /PHY3/MDIO -> /PHY1/MDIO
- U1102 pad 31: /PHY3/MDC -> /PHY1/MDC
- U1102 pad 32: /PHY3/PHY_3V3 -> /PHY1/PHY_3V3
- U1102 pad 33: /PHY3/CLK_X2 -> /PHY1/CLK_X2
- U1102 pad 34: /PHY3/CLK_X1 -> /PHY1/CLK_X1
- U1102 pad 37: Net-(C1104-Pad1) -> Net-(C1107-Pad1)
- U1102 pad 39: /FPGA/PHY3_RX_DV -> /FPGA/PHY1_RX_DV
- U1102 pad 4: /FPGA/PHY3_TXD_1 -> /FPGA/PHY1_TXD_1
- U1102 pad 40: /PHY3/CRS_DV -> /PHY1/CRS_DV
- U1102 pad 41: /PHY3/MDIX_EN -> /PHY1/MDIX_EN
- U1102 pad 42: /PHY3/PHY_AD0 -> /PHY1/PHY_AD0
- U1102 pad 43: /FPGA/PHY3_RXD_0 -> /FPGA/PHY1_RXD_0
- U1102 pad 44: /FPGA/PHY3_RXD_1 -> /FPGA/PHY1_RXD_1
- U1102 pad 45: /PHY3/PHY_AD3 -> /PHY1/PHY_AD3
- U1102 pad 46: /PHY3/PHY_AD4 -> /PHY1/PHY_AD4
- U1102 pad 48: /PHY3/PHY_3V3 -> /PHY1/PHY_3V3
- U1102 pad 6: /PHY3/SNI_MODE -> /PHY1/SNI_MODE
- U1102 pad 7: /FPGA/PHY3_POWER_DOWN -> /FPGA/PHY1_POWER_DOWN
- U602 pad 5: Net-(U602-Pad5) -> Net-(D602-Pad2)
- U602 pad 80: Net-(D602-Pad2) -> Net-(U602-Pad80)
- U701 pad 1: Net-(R701-Pad1) -> GNDD
- U701 pad 2: Net-(C717-Pad1) -> /100BASETX-PHY 1/PHY_3V3
- U702 pad 1: GNDD -> Net-(U702-Pad1)
- U702 pad 2: Net-(C718-Pad1) -> /STM32/PHY_TX_EN
- U702 pad 3: +5V -> /STM32/PHY_TXD_0
- U801 pad 2: /100BASETX-PHY 1/PHY_3V3 -> /PHY3/PHY_3V3
- U802 pad 13: /100BASETX-PHY 1/RX- -> /PHY3/RX-
- U802 pad 14: /100BASETX-PHY 1/RX+ -> /PHY3/RX+
- U802 pad 16: /100BASETX-PHY 1/TD- -> /PHY3/TD-
- U802 pad 17: /100BASETX-PHY 1/TD+ -> /PHY3/TD+
- U802 pad 18: Net-(C805-Pad1) -> Net-(C808-Pad1)
- U802 pad 2: /STM32/PHY_TX_EN -> /FPGA/PHY3_TX_EN
- U802 pad 20: Net-(R819-Pad2) -> Net-(R804-Pad2)
- U802 pad 22: /100BASETX-PHY 1/PHY_3V3 -> /PHY3/PHY_3V3
- U802 pad 23: Net-(C807-Pad1) -> Net-(C810-Pad1)
- U802 pad 24: Net-(R821-Pad2) -> Net-(R806-Pad2)
- U802 pad 25: /100BASETX-PHY 1/CLK_OUT -> /PHY3/CLK_OUT
- U802 pad 26: /100BASETX-PHY 1/AN_EN -> /PHY3/AN_EN
- U802 pad 27: /100BASETX-PHY 1/AN1 -> /PHY3/AN1
- U802 pad 28: /100BASETX-PHY 1/AN0 -> /PHY3/AN0
- U802 pad 29: /100BASETX-PHY 1/~RESET -> /FPGA/~PHY3_RESET
- U802 pad 3: /STM32/PHY_TXD_0 -> /FPGA/PHY3_TXD_0
- U802 pad 30: /100BASETX-PHY 1/MDIO -> /PHY3/MDIO
- U802 pad 31: /100BASETX-PHY 1/MDC -> /PHY3/MDC
- U802 pad 32: /100BASETX-PHY 1/PHY_3V3 -> /PHY3/PHY_3V3
- U802 pad 33: /100BASETX-PHY 1/CLK_X2 -> /PHY3/CLK_X2
- U802 pad 34: /FPGA/CLK_IN -> /PHY3/CLK_X1
- U802 pad 37: Net-(C804-Pad1) -> Net-(C807-Pad1)
- U802 pad 39: /100BASETX-PHY 1/RX_DV -> /FPGA/PHY3_RX_DV
- U802 pad 4: /STM32/PHY_TXD_1 -> /FPGA/PHY3_TXD_1
- U802 pad 40: /100BASETX-PHY 1/CRS_DV -> /PHY3/CRS_DV
- U802 pad 41: /100BASETX-PHY 1/MDIX_EN -> /PHY3/MDIX_EN
- U802 pad 42: /100BASETX-PHY 1/PHY_AD0 -> /PHY3/PHY_AD0
- U802 pad 43: /STM32/PHY_RXD_0 -> /FPGA/PHY3_RXD_0
- U802 pad 44: /STM32/PHY_RXD_1 -> /FPGA/PHY3_RXD_1
- U802 pad 45: /100BASETX-PHY 1/PHY_AD3 -> /PHY3/PHY_AD3
- U802 pad 46: /100BASETX-PHY 1/PHY_AD4 -> /PHY3/PHY_AD4
- U802 pad 48: /100BASETX-PHY 1/PHY_3V3 -> /PHY3/PHY_3V3
- U802 pad 6: /100BASETX-PHY 1/SNI_MODE -> /PHY3/SNI_MODE
- U802 pad 7: /100BASETX-PHY 1/POWER_DOWN -> /FPGA/PHY3_POWER_DOWN
- Y501 pad 2: Net-(C503-Pad1) -> GNDD
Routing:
- net /FPGA/VCCO_3V3: track 143.0 -> 41.3 mm, vias 44 -> 0
- net /FPGA/VCCINT_1V2: track 80.6 -> 12.4 mm, vias 5 -> 0
- net Net-(R1143-Pad1): track 59.7 -> 0.00 mm, vias 2 -> 0
- net +5V: track 75.7 -> 16.4 mm, vias 29 -> 0
- net Net-(R1144-Pad1): track 57.0 -> 0.00 mm, vias 2 -> 0
- net Net-(R1145-Pad1): track 55.7 -> 0.00 mm, vias 2 -> 0
- net Net-(R1146-Pad1): track 53.5 -> 0.00 mm, vias 2 -> 0
- net GNDD: track 88.9 -> 40.6 mm, vias 325 -> 68
- net /FPGA/CSO_B: track 41.8 -> 1.63 mm, vias 2 -> 0
- net /100BASETX-PHY 1/PHY_3V3: track 62.3 -> 23.9 mm, vias 20 -> 19
- net /PHY2/PHY_3V3: track 62.2 -> 24.6 mm, vias 20 -> 19
- net Net-(Q202-Pad2): track 7.34 -> 43.9 mm, vias 0 -> 2
- net /PHY1/PHY_3V3: track 61.2 -> 24.7 mm, vias 20 -> 19
- net /PHY3/PHY_3V3: track 60.5 -> 24.6 mm, vias 20 -> 19
- net /STM32/PHY_TXD_1: track 44.4 -> 11.5 mm, vias 2 -> 0
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- added copper zone on F.Cu, net Net-(C1124-Pad1)
- added copper zone on F.Cu, net Net-(C1125-Pad1)
- removed copper zone on In2.Cu, net +5V
- removed copper zone on In2.Cu, net /FPGA/VCCO_3V3
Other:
- board size 120 x 117 mm -> 100 x 100 mm
- net class Default: trace_width 0.25 -> 0.2
- net class Small added: clearance 0.2, trace_width 0.15, via_dia 0.8, via_drill 0.4
- rule trace_min: 0 -> 0.15
- board text removed: "3V3"
- board text removed: "ADC1"
- board text removed: "ADC2"
- board text removed: "BOOT0"
- board text removed: "BOOT1"
- board text removed: "Christopher Simon"
- board text removed: "Ethernet Sniffer v0.01"
- board text removed: "FPGA 100BASE-TX 1"
- board text removed: "FPGA 100BASE-TX 2"
- board text removed: "FPGA 100BASE-TX 3"
- board text removed: "GND"
- board text removed: "JTAG"
- board text removed: "PD0-7"
- board text removed: "SDA"
- board text removed: "SDL"
- board text removed: "STM32 100BASE-TX"
- board text removed: "SWD"
- board text removed: "UART RX"
- board text removed: "UART TX"
